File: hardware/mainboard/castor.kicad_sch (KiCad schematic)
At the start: 46 parts, among them J7 OSC OUT, Q1 MMBT3906, U10 MCP6001-OT, U7 TL074, U8 TL074, U9 74LVC2G74

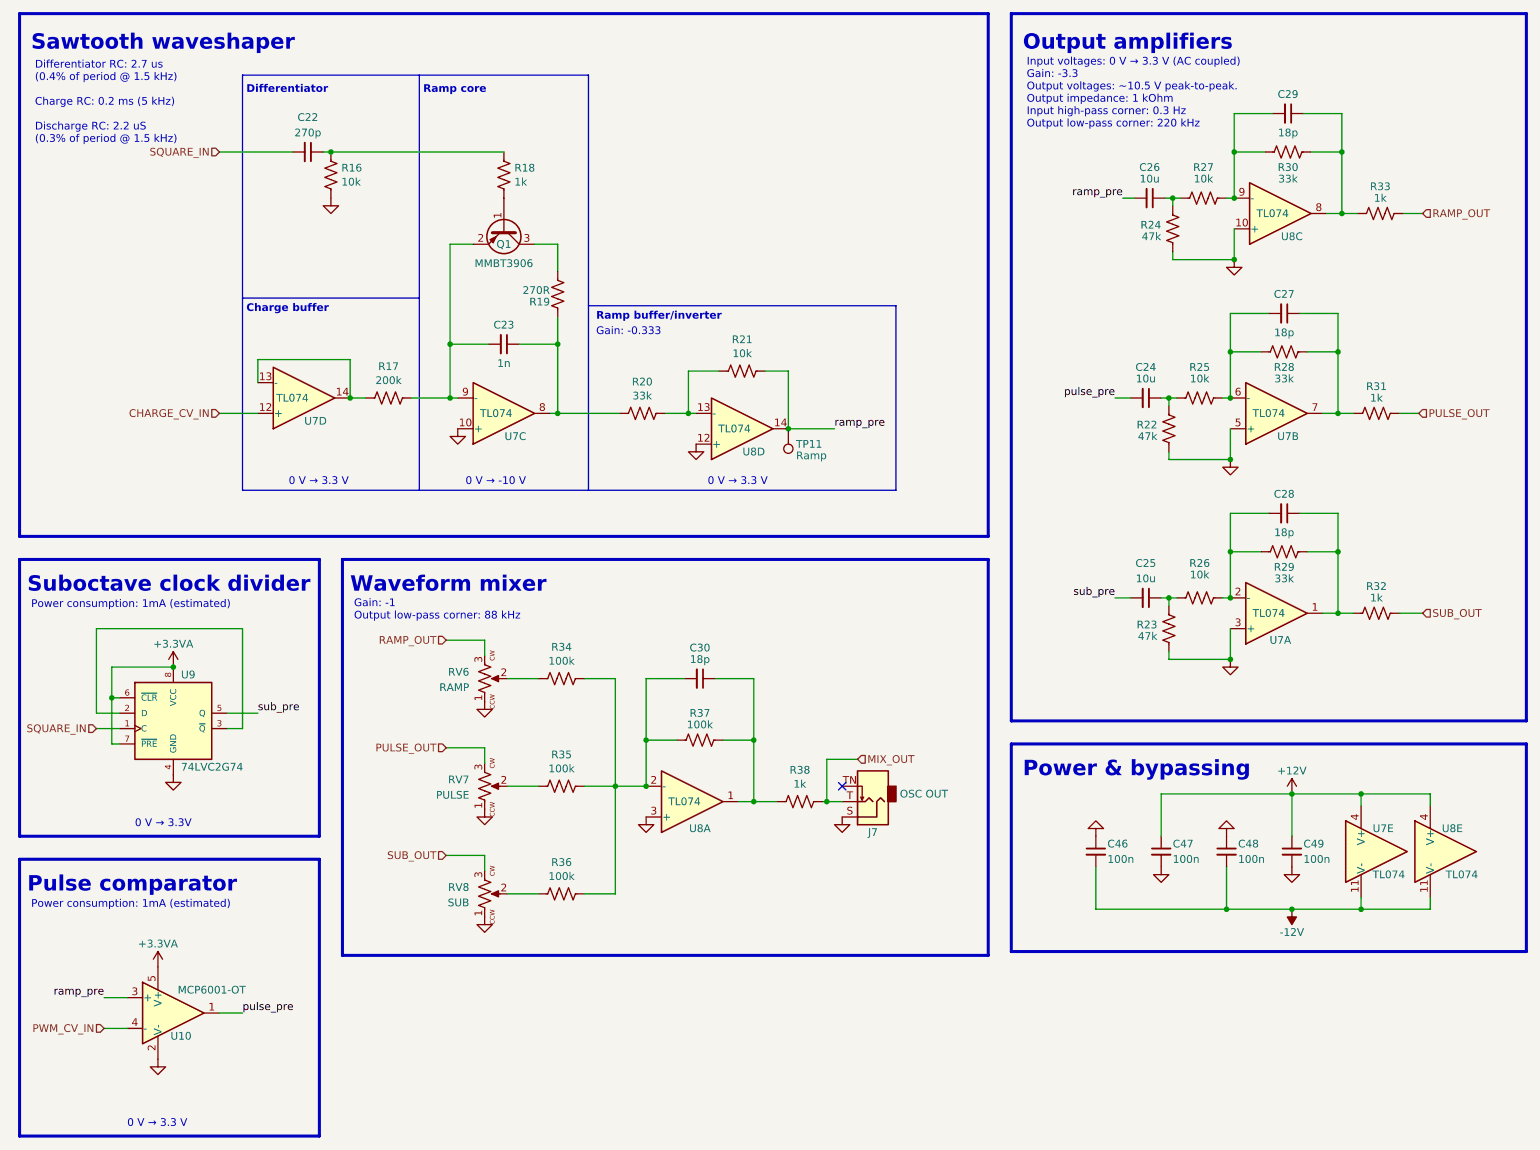
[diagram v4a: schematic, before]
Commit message: hardware: add rating field to schematic
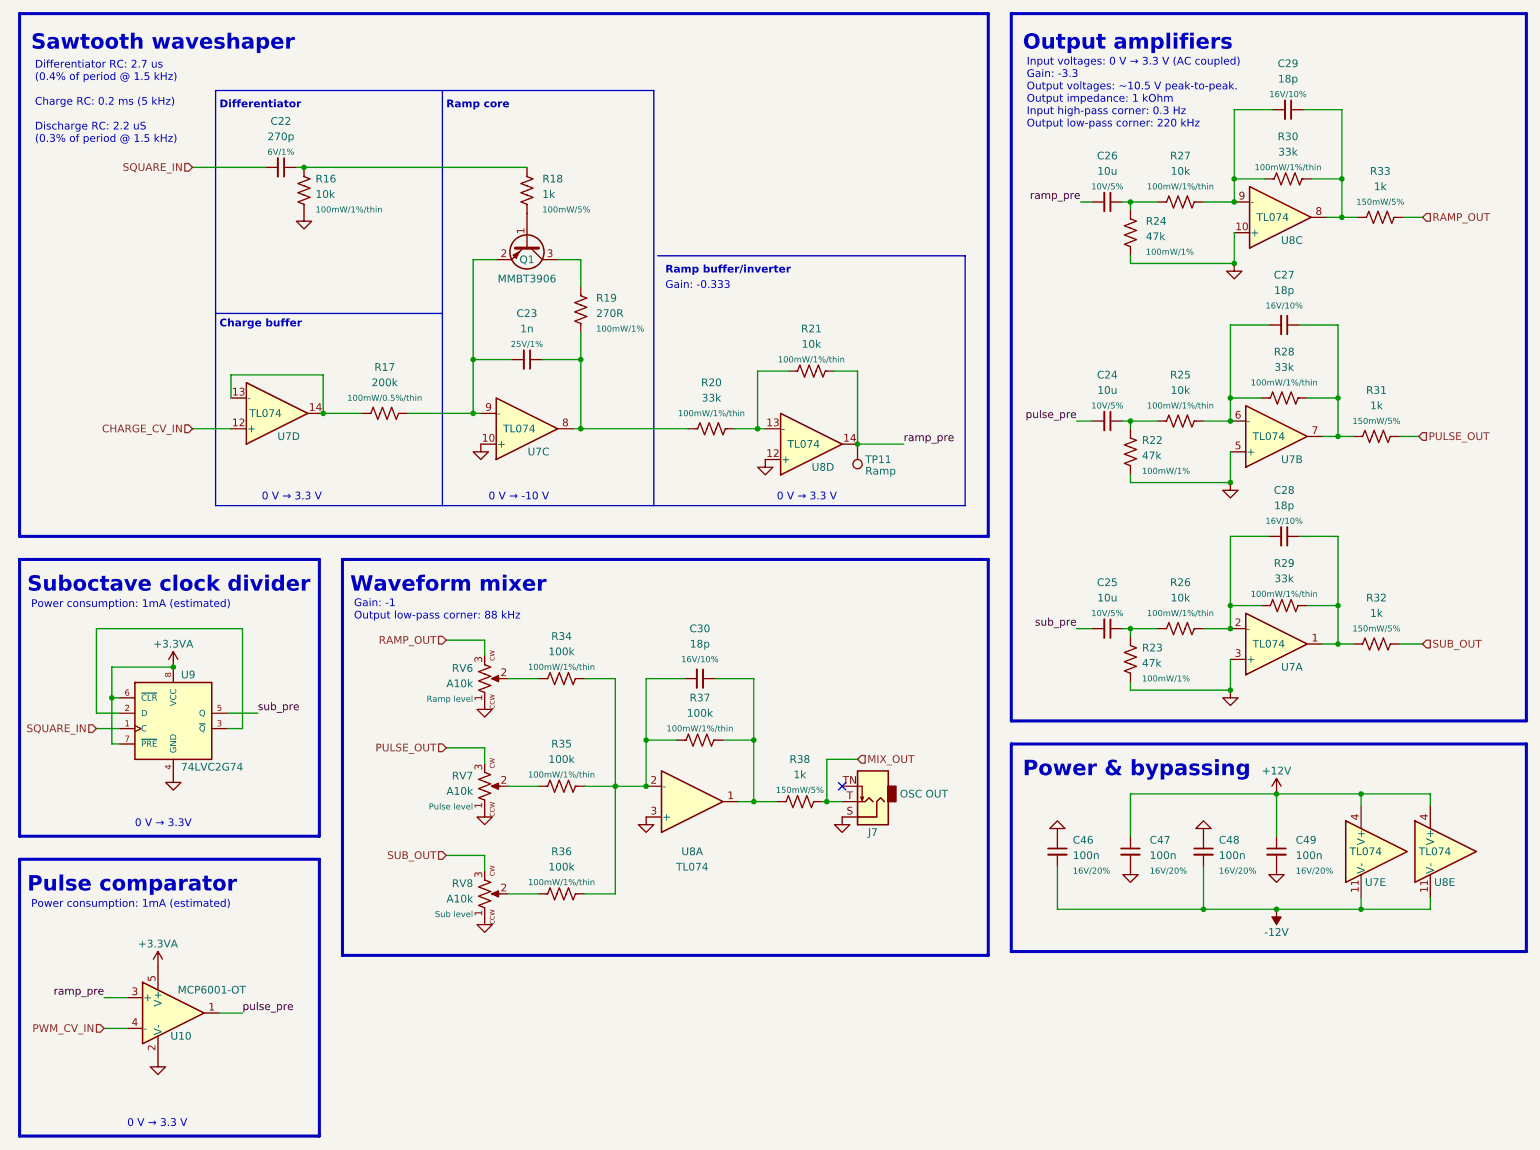
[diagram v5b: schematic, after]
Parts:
- C22: Rating (none) -> 6V/1%
- C23: Rating (none) -> 25V/1%
- C24, C25, C26: Rating (none) -> 10V/5%
- C27, C28, C29, C30: Rating (none) -> 16V/10%
- C46, C47, C48, C49: Rating (none) -> 16V/20%
- R16, R20, R21, R25, R26, R27, R28, R29, R30, R34, R35, R36, R37: Rating (none) -> 100mW/1%/thin
- R17: Rating (none) -> 100mW/0.5%/thin
- R18: Rating (none) -> 100mW/5%
- R19, R22, R23, R24: Rating (none) -> 100mW/1%
- R31, R32, R33, R38: Rating (none) -> 150mW/5%
- RV6: value RAMP -> A10k; Rating (none) -> Ramp level
- RV7: value PULSE -> A10k; Rating (none) -> Pulse level
- RV8: value SUB -> A10k; Rating (none) -> Sub level
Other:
- moved on the sheet: C22, C23, C24, C25, C26, C27, C28, C29, C46, C47, C48, C49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

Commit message: hardware: fixup schematic fields
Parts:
- C22: MPN (none) -> GCM1555C1H271FA16D; Notes (none) -> Ramp core; Reqs Ramp core, C0G 1% or better, 6 V -> (none); finalized yes -> (none); mpn GCM1555C1H271FA16D -> (none)
- C23: MPN (none) -> GCM1555C1H102FA16D, GRM1555C1H102FA01D; Notes (none) -> Ramp core; Reqs Ramp core, C0G 1% or better, 25 V -> (none); finalized yes -> (none); mpn GCM1555C1H102FA16D, GRM1555C1H102FA01D -> (none)
- C24, C25, C26: MPN (none) -> CL10A106MP8NNNC; Notes (none) -> Low voltage audio, 10 V; Reqs Low voltage audio, 10 V -> (none); finalized yes -> (none); mpn CL10A106MP8NNNC -> (none)
- C27, C28, C29, C30: MPN (none) -> CL05C180JB5NNNC; Notes (none) -> Eurorack level audio filter; Reqs Eurorack level audio filter, 16 V -> (none); finalized yes -> (none); mpn CL05C180JB5NNNC -> (none)
- C46, C47, C48, C49: MPN (none) -> CL05B104KO5NNNC; MacroFab MPN (none) -> MF-CAP-0402-0.1uF; Notes (none) -> Bypass; Reqs Bypass, 16 V -> (none); finalized yes -> (none); macrofab_mpn MF-CAP-0402-0.1uF -> (none); mpn CL05B104KO5NNNC -> (none)
- J7: MPN (none) -> WQP-WQP518MA; finalized yes -> (none); mpn WQP-WQP518MA -> (none)
- Q1: MPN (none) -> MMBT3906L; MacroFab MPN (none) -> MF-DSC-SOT233-MMBT3906; macrofab_mpn MF-DSC-SOT233-MMBT3906 -> (none); mpn MMBT3906L -> (none)
- R16: MPN (none) -> RR0510P-103-D; Notes (none) -> Digital control path; Reqs Digital control path, 1%, 100 mW, thin film -> (none); mpn RR0510P-103-D -> (none)
- R17: MPN (none) -> RC0402FR-07200KL; Notes (none) -> Analog control path; Reqs Analog control path, 0.5%, 100 mW, thin film -> (none); mpn RC0402FR-07200KL -> (none)
- R18: MPN (none) -> RC0402JR-071KL; Notes (none) -> Digital control path; Reqs Digital control path, 5%, 100 mW, thin film -> (none); mpn RC0402JR-071KL -> (none)
- R19: MPN (none) -> CRGCQ0402F270R; Notes (none) -> Ramp core; Reqs Ramp core, 1%, 100 mW, thin film -> (none); mpn CRGCQ0402F270R -> (none)
- R20: MPN (none) -> RC0402FR-0733KL; Notes (none) -> Low voltage audio; Reqs Low voltage audio, 1%, 100 mW, thin film -> (none); mpn RC0402FR-0733KL -> (none)
- R21, R25, R26, R27: MPN (none) -> RR0510P-103-D; Notes (none) -> Low voltage audio; Reqs Low voltage audio, 1%, 100 mW, thin film -> (none); mpn RR0510P-103-D -> (none)
- R22, R23, R24: MPN (none) -> RC0402FR-0747KL; Notes (none) -> Low voltage audio; Reqs Low voltage audio, 1%, 100, thin film -> (none); mpn RC0402FR-0747KL -> (none)
- R28, R29, R30: MPN (none) -> RC0402FR-0733KL; Notes (none) -> Eurorack level audio; Reqs Eurorack level audio, 1%, 100 mW, thin film -> (none); mpn RC0402FR-0733KL -> (none)
- R31, R32, R33, R38: MPN (none) -> MCT06030C1001FP500, ERA-3AEB102V; Notes (none) -> Eurorack level audio, output impedance; Reqs Output impedance, 5%, 150 mW, thin film -> (none); mpn MCT06030C1001FP500, ERA-3AEB102V -> (none)
- R34, R35, R36, R37: MPN (none) -> RC0402DR-07100KL; Notes (none) -> Eurorack level audio; Reqs Eurorack level audio, 1%, 100 mW, thin film -> (none); mpn RC0402DR-07100KL -> (none)
- RV6, RV7, RV8: MPN (none) -> R0904N-B10K L-25KQ/LWS; Notes (none) -> linear or audio taper, 9mm tall trimmer pot with white indi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; Reqs 10k, linear or audio taper, 9mm tall trimmer pot with white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 -> (none); finalized yes -> (none); mpn R0904N-B10K L-25KQ/LWS -> (none)
- TP11: DNP (none) -> 1; dnp 1 -> (none); finalized n/a -> (none)
- U10: MPN (none) -> MCP6001T-I/OT, AD8541ARTZ; finalized yes -> (none); mpn MCP6001T-I/OT, AD8541ARTZ -> (none)
- U7, U8: MPN (none) -> TL074CPW; finalized yes -> (none); mpn TL074CPW -> (none)
- U9: MPN (none) -> 74LVC2G74DP,125; finalized yes -> (none); mpn 74LVC2G74DP,125 -> (none)

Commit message: hardware: use winterbloom footprints for C, R, and L
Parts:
- C22, C23, C27, C28, C29, C30, C46, C47, C48, C49: footprint Capacitor_SMD:C_0402_1005Metric_Pad0.74x0.62mm_HandSolder -> winterbloom:C_0402_HandSolder
- C24, C25, C26: footprint Capacitor_SMD:C_0603_1608Metric_Pad1.08x0.95mm_HandSolder -> winterbloom:C_0603_HandSolder
- R16, R17, R18, R19, R20, R21, R22, R23, R24, R25, R26, R27, R28, R29, R30, R34, R35, R36, R37: footprint Resistor_SMD:R_0402_1005Metric_Pad0.72x0.64mm_HandSolder -> winterbloom:R_0402_HandSolder
- R31, R32, R33, R38: footprint Resistor_SMD:R_0603_1608Metric_Pad0.98x0.95mm_HandSolder -> winterbloom:R_0603_HandSolder
